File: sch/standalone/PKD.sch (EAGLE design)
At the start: 30 parts, among them IC1 LM393N, IC2 TL084P, IC3 PIC12F683P, IC4 74HC244N, Q1 BS170

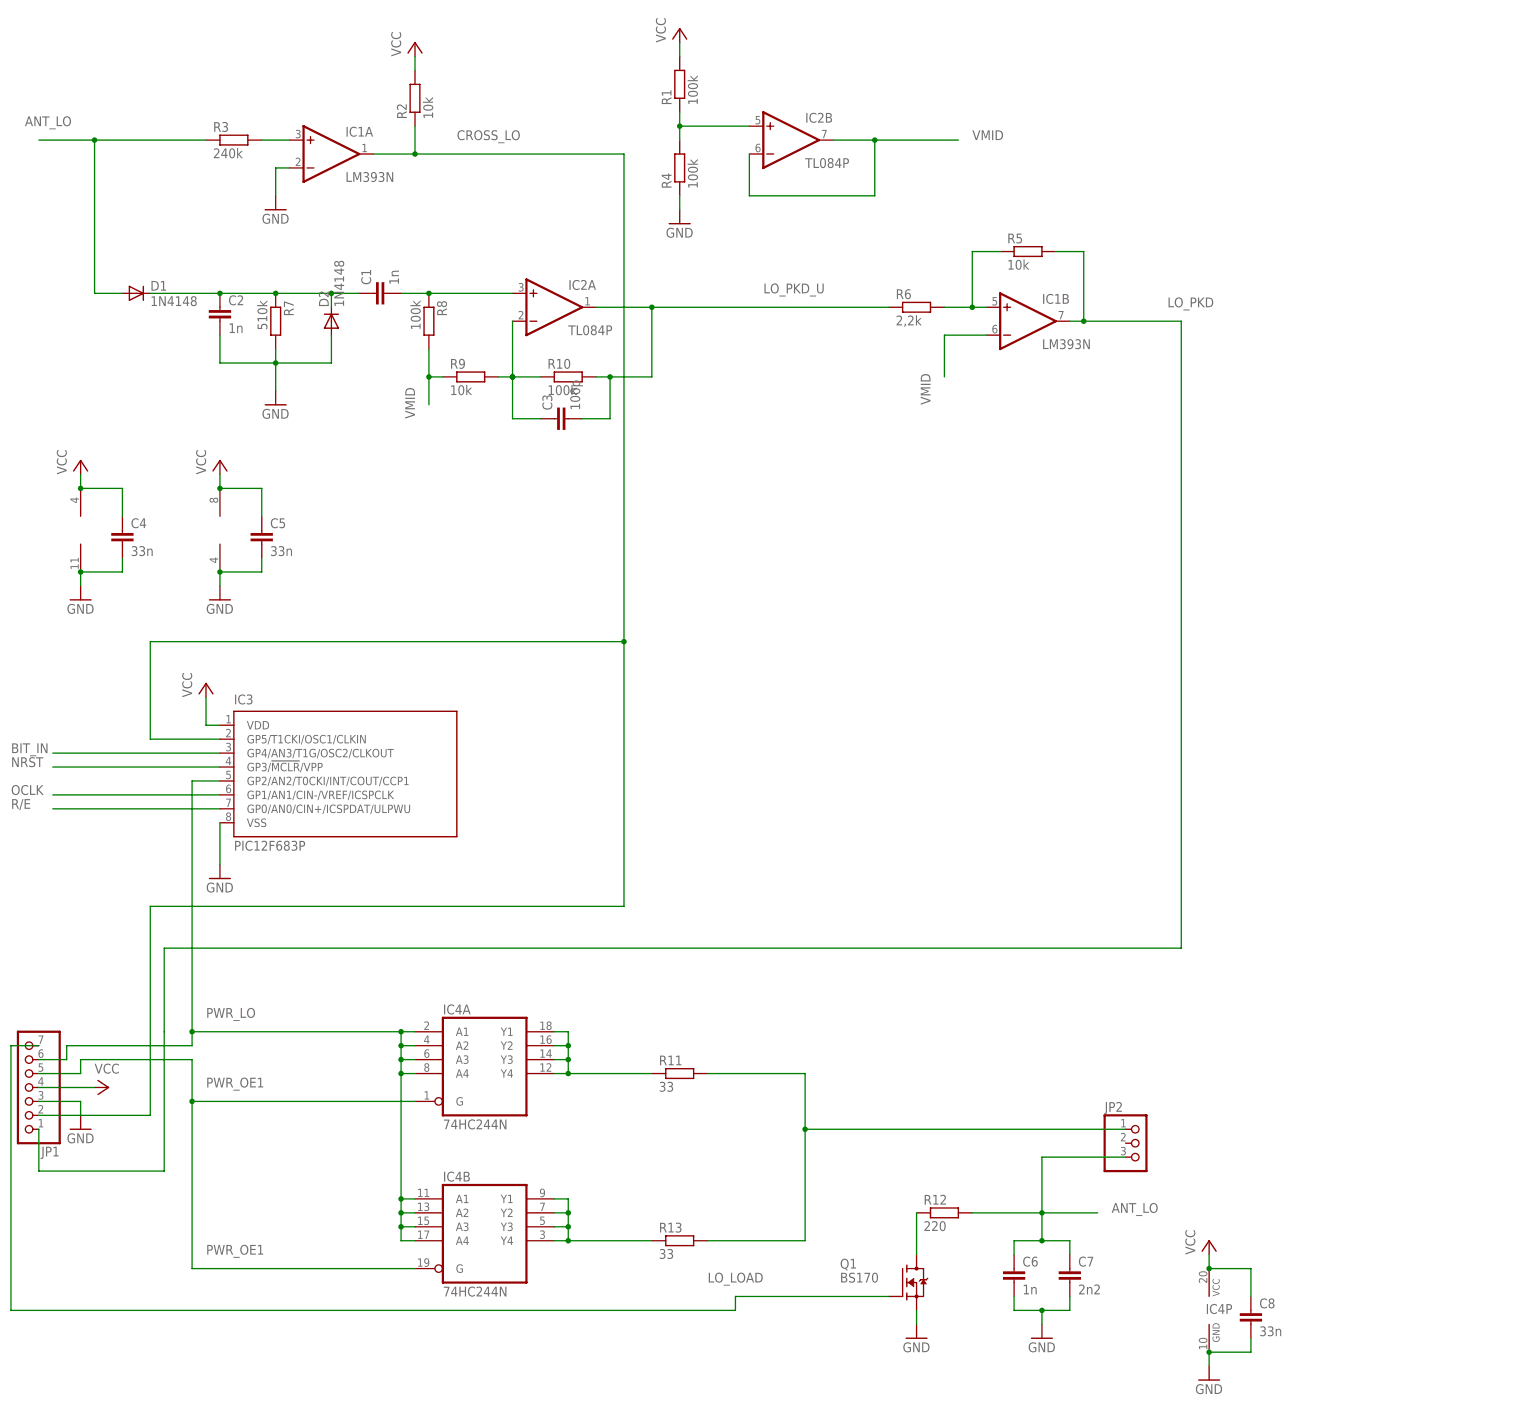
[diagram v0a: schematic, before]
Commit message: Reader + emulator working, modified (reduced) schematics for standalone ver
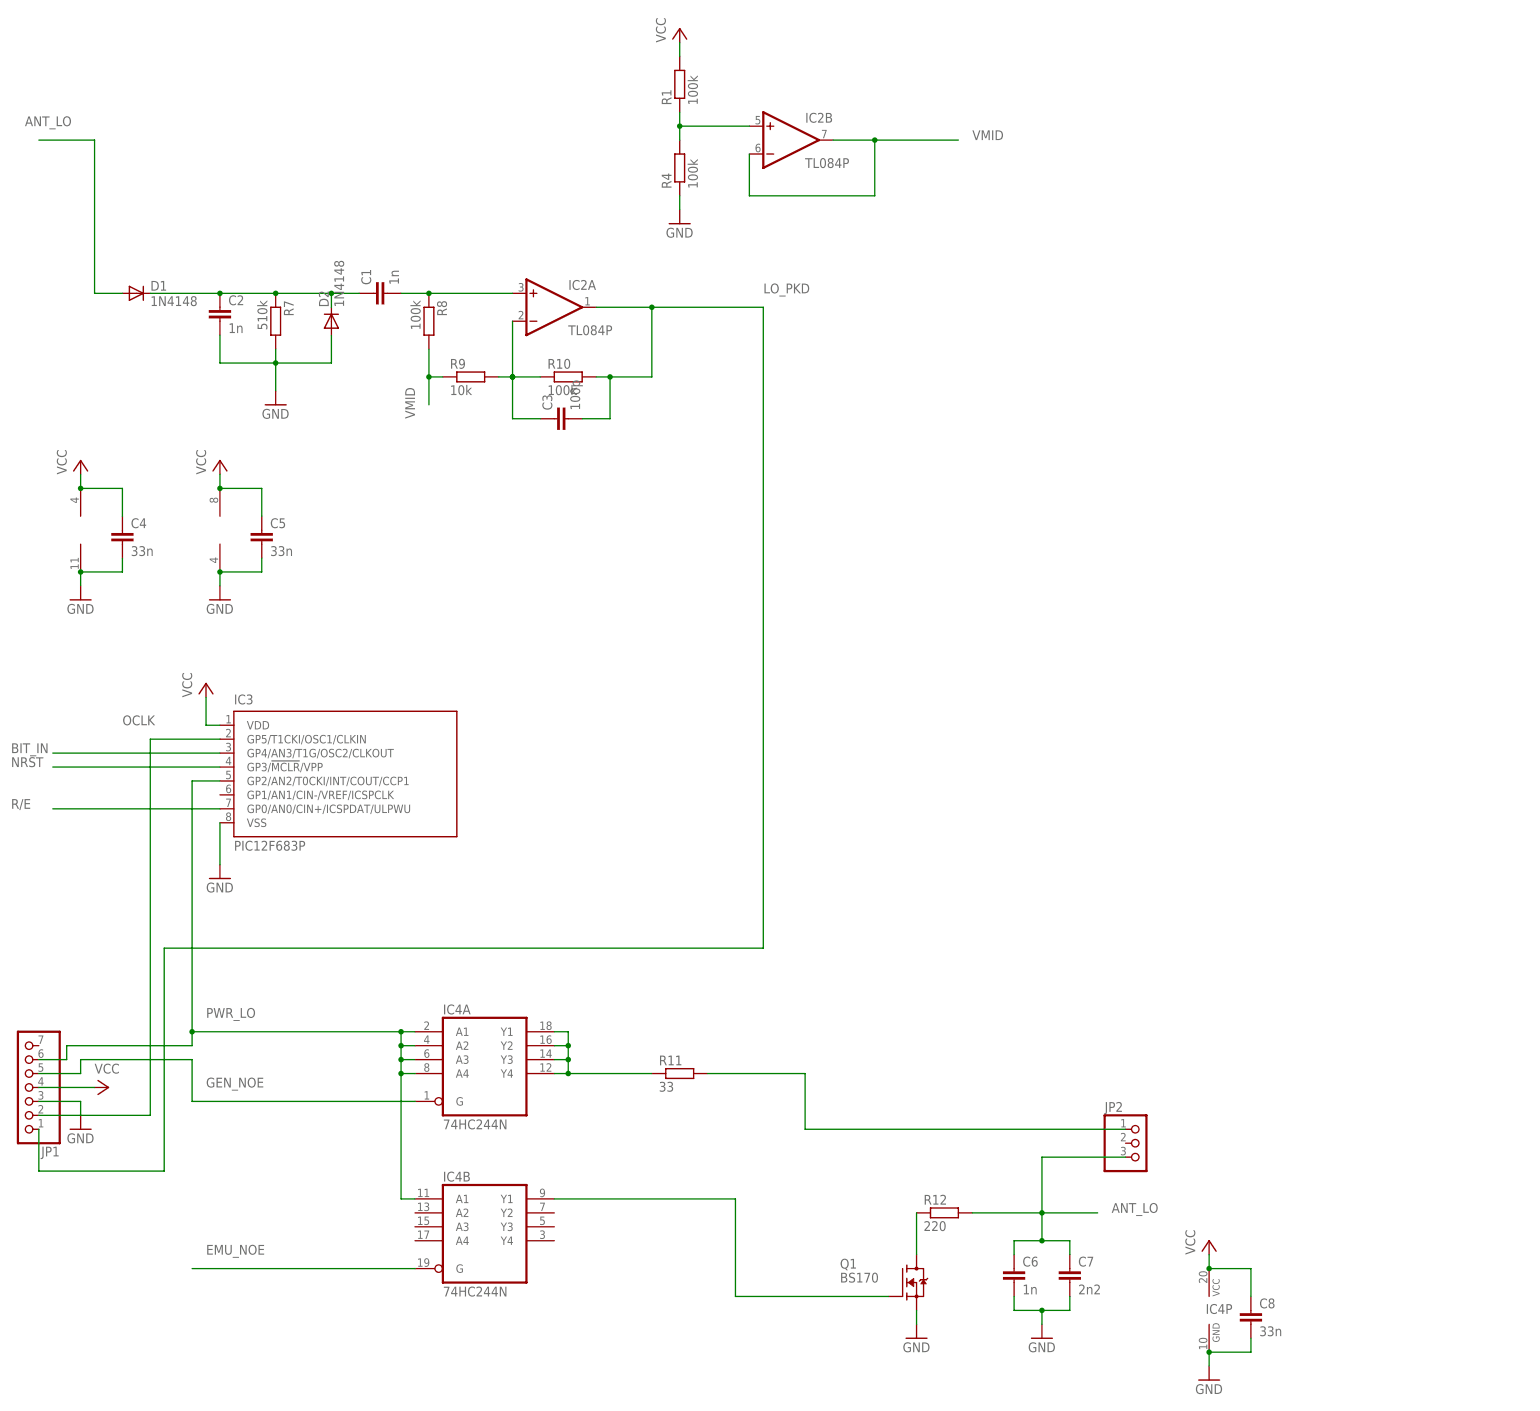
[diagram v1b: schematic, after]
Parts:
- removed R13: 33, rcl:R-EU_0207/10
- removed R2, R5: 10k, rcl:R-EU_0207/10
- removed R3: 240k, rcl:R-EU_0207/10
- removed R6: 2,2k, rcl:R-EU_0207/10
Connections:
- removed net CROSS_LO: IC1A.OUT, IC3.GP5/T1CKI/OSC1/CLKIN, JP1.2, R2.1
- removed net LO_LOAD: JP1.7, Q1.G
- removed net LO_PKD_U: C3.2, IC2A.OUT, R10.2, R6.1
- removed net N$15: IC4B.Y1, IC4B.Y2, IC4B.Y3, IC4B.Y4, R13.1
- removed net N$17: IC1B.+IN, R5.1, R6.2
- removed net N$6: IC1A.+IN, R3.2
- removed net PWR_OE1: IC4A.G, IC4B.G, JP1.5
- new net EMU_NOE: IC4B.G
- new net GEN_NOE: IC4A.G, JP1.5
- new net N$7: IC4B.Y1, Q1.G
- net ANT_LO: no longer R3.1
- net GND: no longer IC1A.-IN
- net LO_PKD: now also C3.2, IC2A.OUT, R10.2; no longer IC1B.OUT, R5.2
- net N$13: no longer R13.2
- net OCLK: now also IC3.GP5/T1CKI/OSC1/CLKIN, JP1.2; no longer IC3.GP1/AN1/CIN-/VREF/ICSPCLK
- net PWR_LO: no longer IC4B.A2, IC4B.A3, IC4B.A4
- net VCC: no longer R2.2
- net VMID: no longer IC1B.-IN

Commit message: Minor update
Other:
- note added: "Antenna Connector"
- moved on the sheet: C1, C2, C3, C4, C5, C6, C7, C8, D1, D2, IC2A, IC2B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
